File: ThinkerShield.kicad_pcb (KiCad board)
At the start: 2 copper layers, 69 x 69 mm, 40 parts, among them SW1 SW_PUSHBUTTON, SW2 SW_PUSHBUTTON, U1 BUZZER

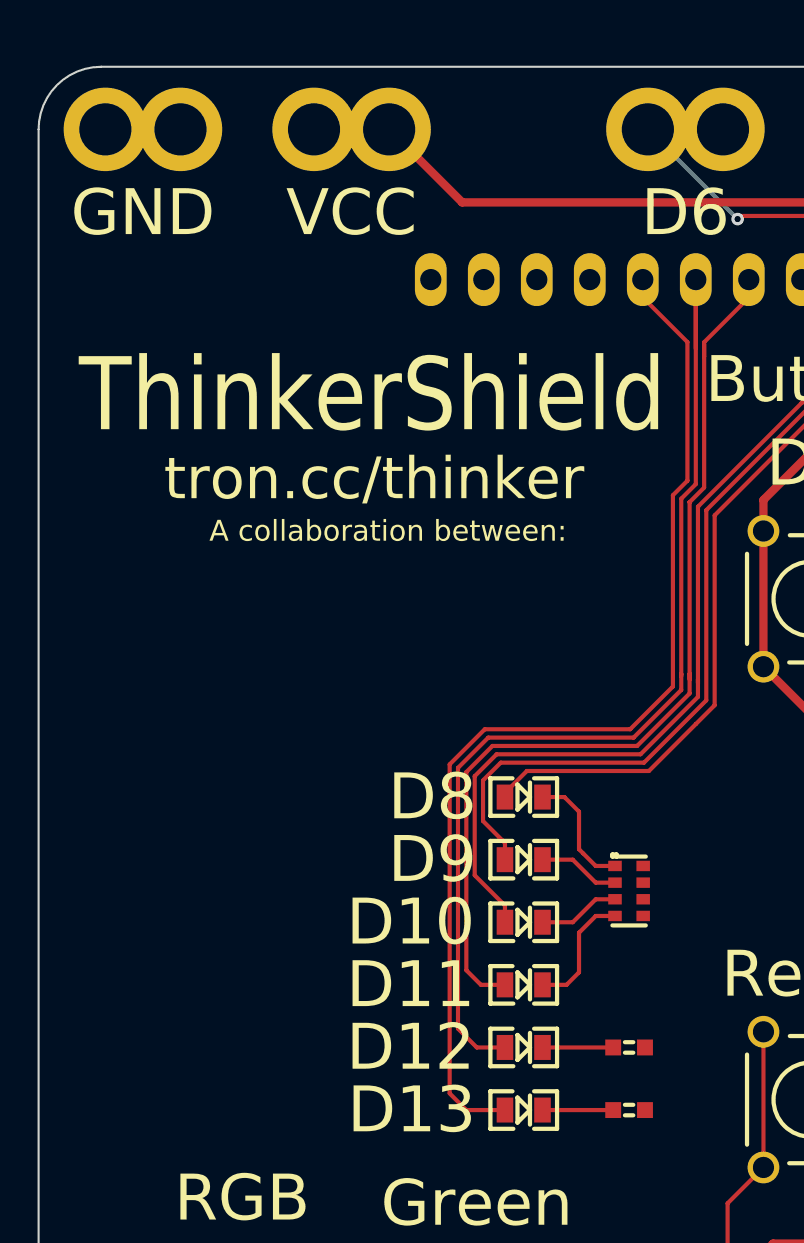
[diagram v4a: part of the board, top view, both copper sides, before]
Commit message: Add power LED
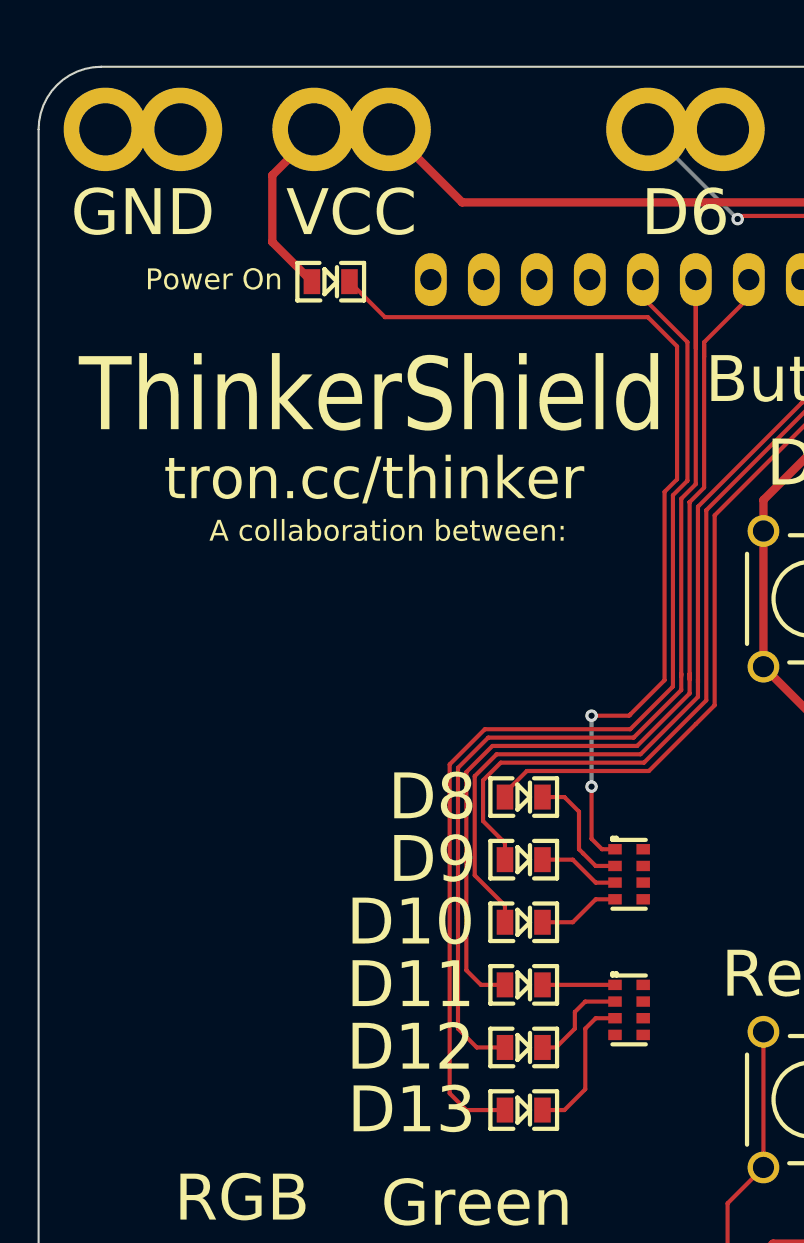
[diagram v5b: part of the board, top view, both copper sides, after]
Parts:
- removed R6: 470R, FT:0603
- added LED7: BLUE, FT:LED-0805, F.Cu at (182.0, 54.3)
- R4: footprint FT:0603 -> FT:RES_CAY16
- moved R4 1.80 mm to (196.3, 89.2), turned to 270 degrees
- moved R3 0.80 mm to (196.3, 82.7)
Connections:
- R3 pad 1: Net-(LED1-PadK) -> Net-(LED7-PadK)
- R3 pad 3: Net-(LED2-PadK) -> Net-(LED1-PadK)
- R3 pad 5: Net-(LED3-PadK) -> Net-(LED2-PadK)
- R3 pad 7: Net-(LED4-PadK) -> Net-(LED3-PadK)
- R4 pad 1: GND -> Net-(LED4-PadK)
- R4 pad 2: Net-(LED5-PadK) -> GND
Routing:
- net Net-(LED7-PadK): track 0.00 -> 44.7 mm, vias 0 -> 2
- net IORef: track 209.9 -> 218.8 mm
- net Net-(LED6-PadK): track 3.39 -> 7.00 mm
- net Net-(LED4-PadK): track 5.96 -> 3.48 mm
- net Net-(LED5-PadK): track 3.39 -> 4.85 mm
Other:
- board text added: "Power On"

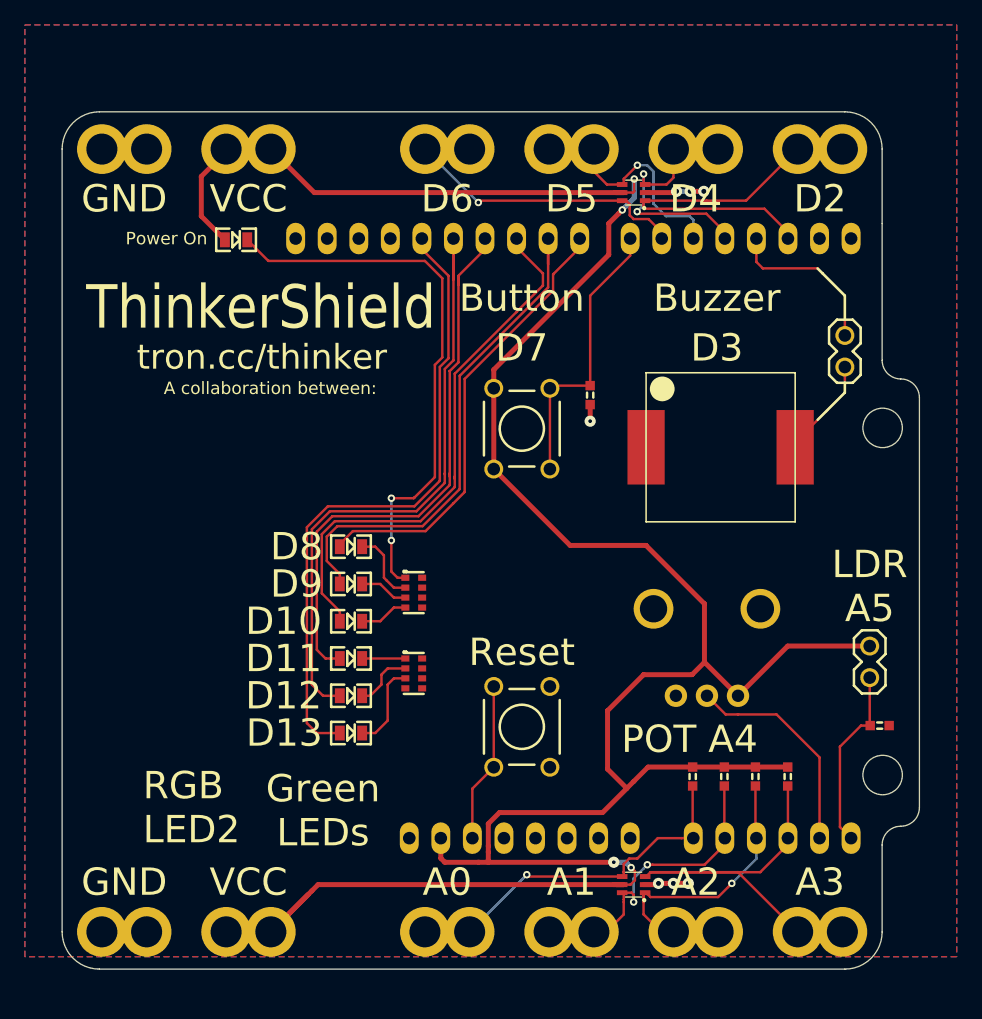
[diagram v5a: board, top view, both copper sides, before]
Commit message: Grow alligator clip holes
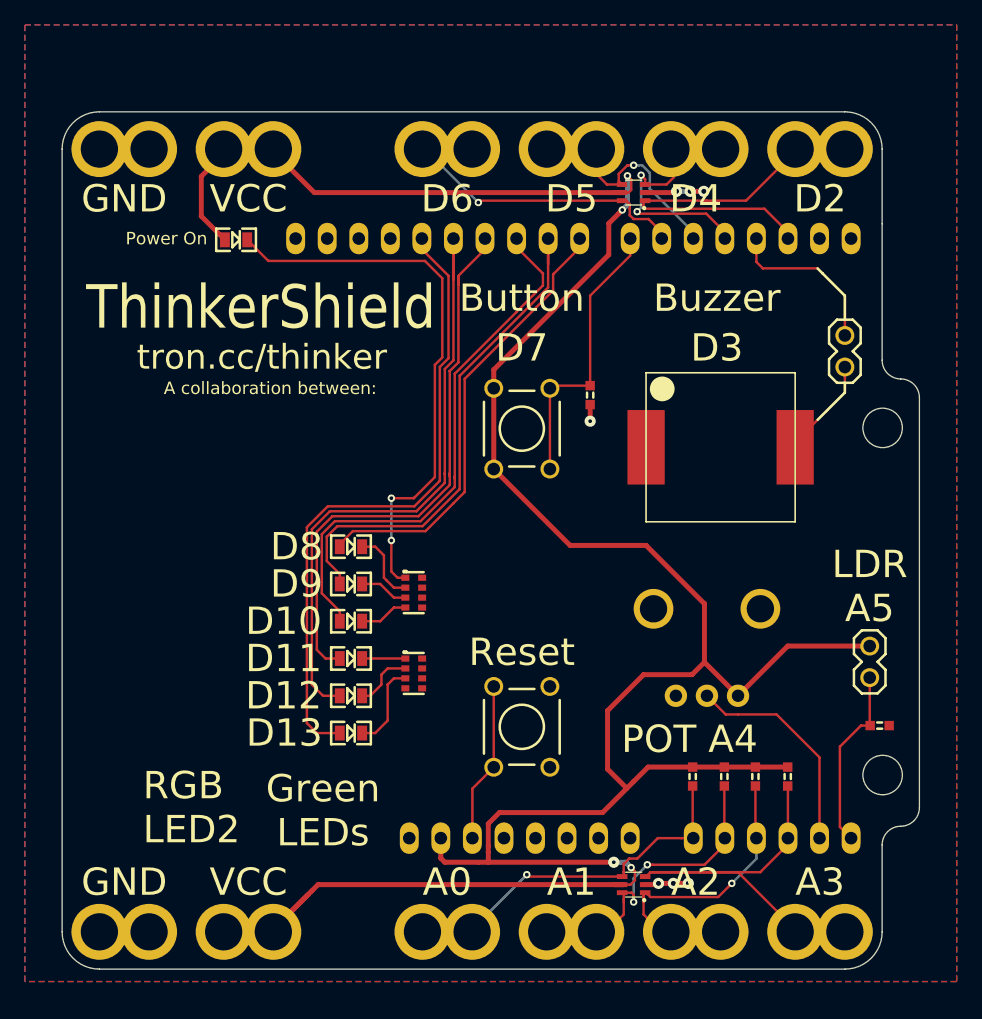
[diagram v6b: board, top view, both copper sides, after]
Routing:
- net /D5: track 20.5 -> 21.9 mm

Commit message: Swap A4/A5 to be compatible with older Thinkup boards
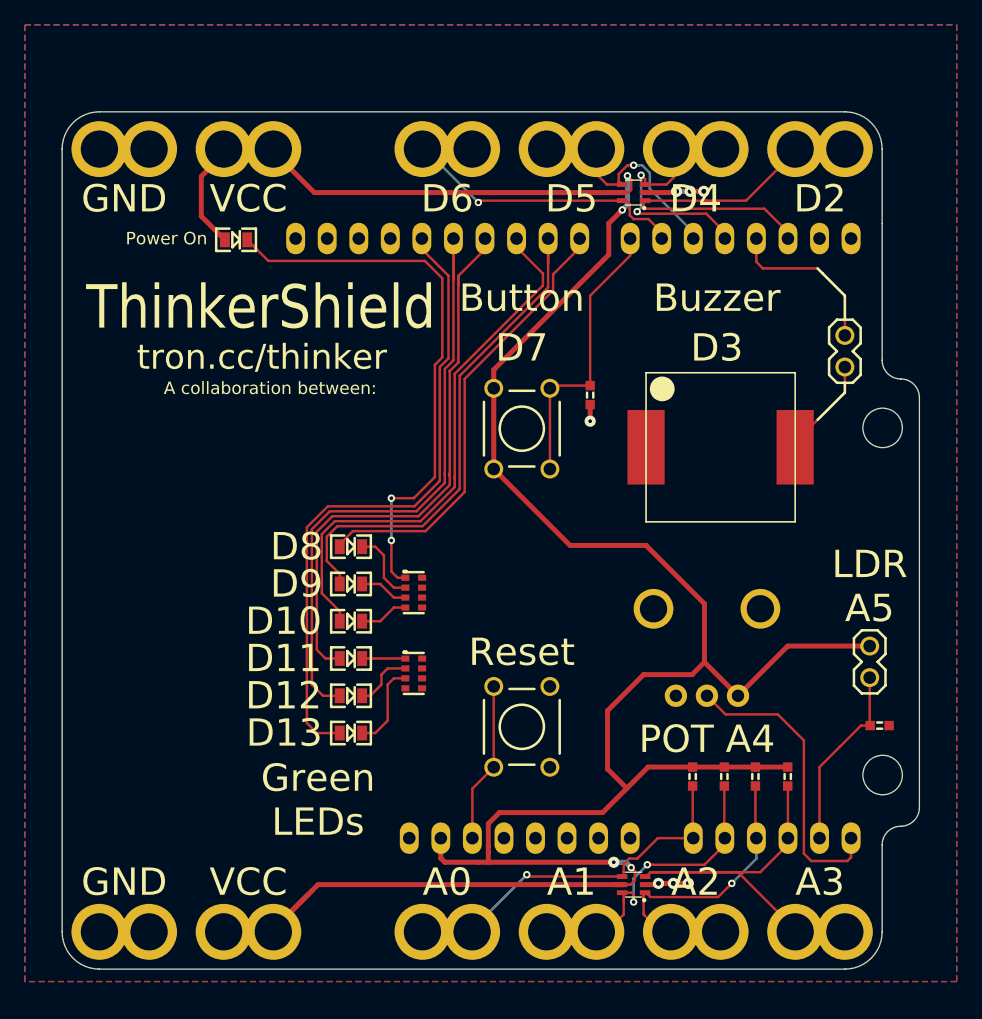
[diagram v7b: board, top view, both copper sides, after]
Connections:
- PH1 pad 2: /A5 -> /A4
- R1 pad 1: /A5 -> /A4
- VR1 pad W: /A4 -> /A5
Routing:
- net /A5: track 14.8 -> 24.1 mm
- net /A4: track 17.6 -> 15.1 mm
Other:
- board text added: "ThinkerShield V1.1"
- board text removed: "RGB LED2"
- board text removed: "ThinkerShield V1.0"

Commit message: Spread out LEDs, use better MAAS logo
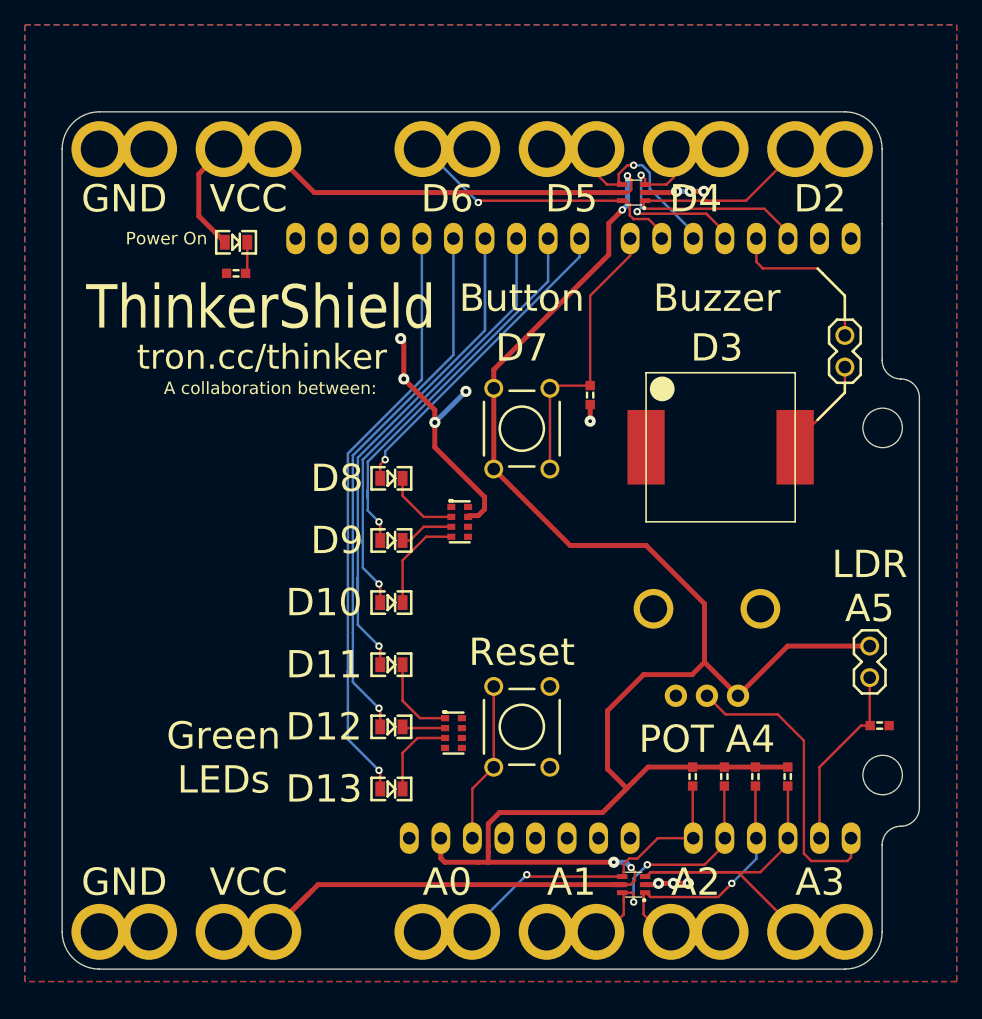
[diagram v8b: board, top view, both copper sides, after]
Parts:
- added R6: 2.2K, FT:0603, F.Cu at (182.0, 57.0)
- moved R3 6.80 mm to (200.0, 77.0)
- moved LED1 6.39 mm to (194.5, 73.5)
- moved R4 5.77 mm to (199.5, 94.0)
- moved LED6 5.55 mm to (194.5, 98.5)
- moved G*** 5.51 mm to (181.8, 64.2)
- moved LED2 4.78 mm to (194.5, 78.5)
- moved LED5 4.10 mm to (194.5, 93.5)
- moved LED3 3.58 mm to (194.5, 83.5)
- moved LED4 3.29 mm to (194.5, 88.5)
- moved LED7 0.20 mm to (182.0, 54.5)
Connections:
- R3 pad 1: Net-(LED7-PadK) -> (no net)
- R3 pad 2: GND -> (no net)
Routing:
- net Net-(LED7-PadK): track 44.7 -> 2.56 mm, vias 2 -> 0
- net GND: track 17.5 -> 39.4 mm, vias 7 -> 11
- net /D9: track 41.7 -> 31.3 mm, vias 0 -> 1
- net /D8: track 37.0 -> 27.4 mm, vias 0 -> 1
- net /D10: track 44.6 -> 36.6 mm, vias 0 -> 1
- net /D12: track 50.7 -> 43.6 mm, vias 0 -> 1
- net /D11: track 47.5 -> 42.7 mm, vias 0 -> 1
- net Net-(LED3-PadK): track 3.93 -> 8.21 mm
- net Net-(LED4-PadK): track 3.48 -> 6.91 mm
- net /D13: track 51.7 -> 49.2 mm, vias 0 -> 1
- net Net-(LED5-PadK): track 4.85 -> 3.47 mm
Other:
- board text removed: "MAAS is a trademark of Museum of Applied Arts and Sciences"
